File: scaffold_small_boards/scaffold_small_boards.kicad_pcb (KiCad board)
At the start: 2 copper layers, 15 x 15 mm, 36 parts

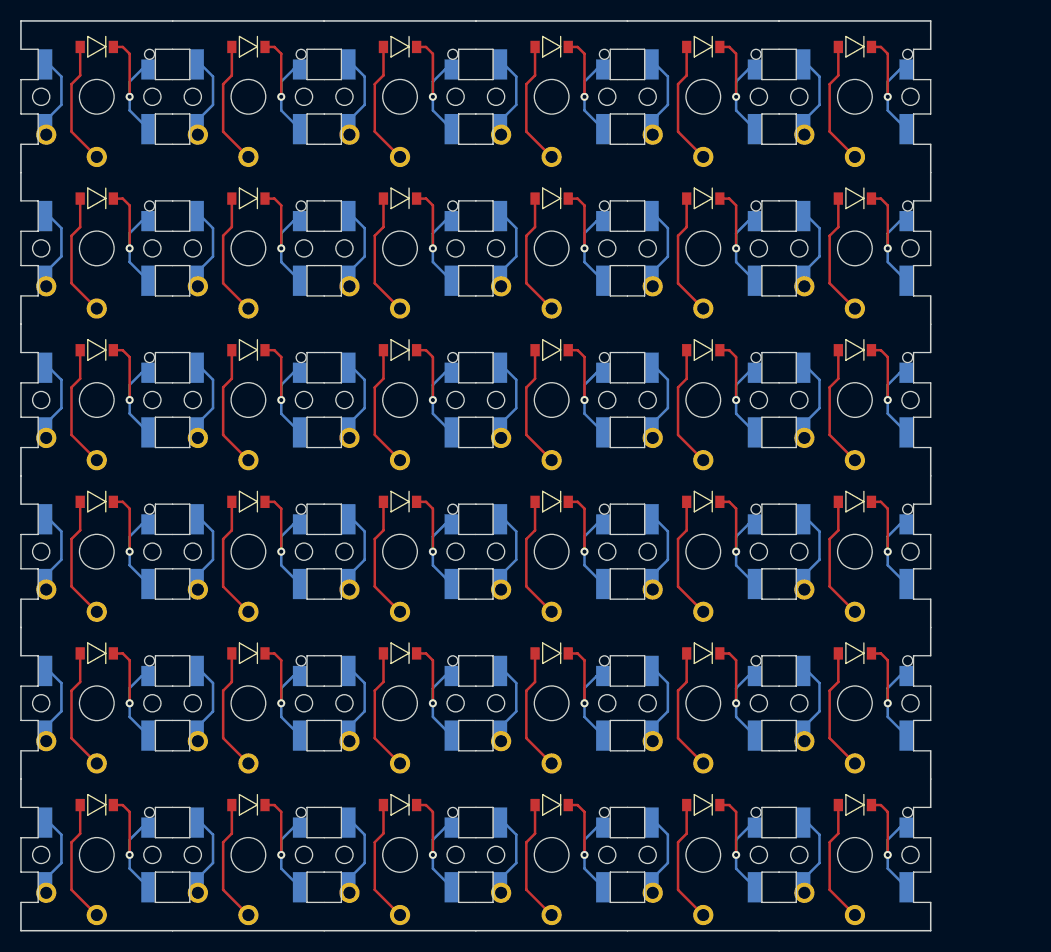
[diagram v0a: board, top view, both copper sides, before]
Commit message: Scaffold V2: wider spacing for supports for better switch fit, updated assembly guide.
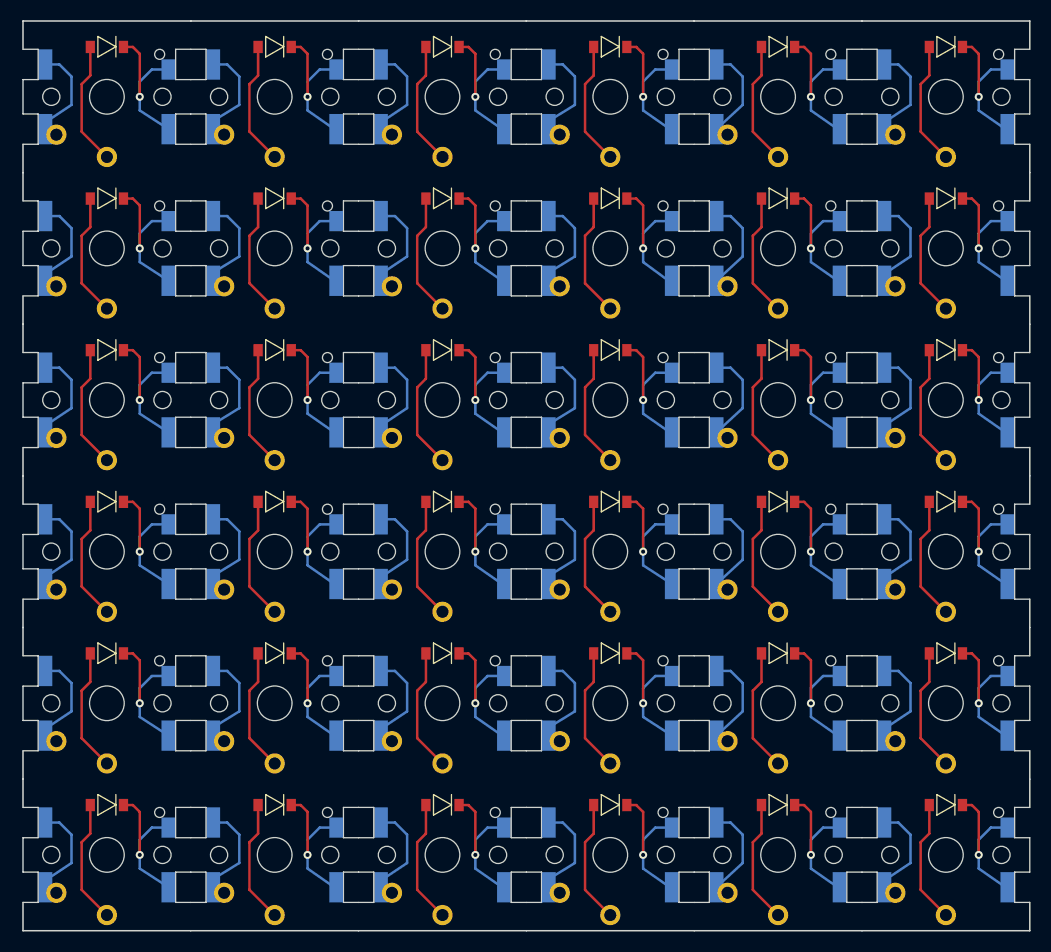
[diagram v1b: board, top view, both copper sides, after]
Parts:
- SW_and_D1: footprint scaffold:Kailh_PG1350_and_sod123_and_cutouts_top_left -> scaffold:Kailh_PG1350_and_sod123_and_cutouts_top_left_v2
- SW_and_D10, SW_and_D15, SW_and_D20, SW_and_D33: footprint scaffold:Kailh_PG1350_and_sod123_and_cutouts_bottom -> scaffold:Kailh_PG1350_and_sod123_and_cutouts_bottom_v2
- SW_and_D11, SW_and_D16, SW_and_D31, SW_and_D6: footprint scaffold:Kailh_PG1350_and_sod123_and_cutouts_top -> scaffold:Kailh_PG1350_and_sod123_and_cutouts_top_v2
- SW_and_D12, SW_and_D13, SW_and_D14, SW_and_D17, SW_and_D18, SW_and_D19, SW_and_D25, SW_and_D26, SW_and_D27, SW_and_D28, SW_and_D29, SW_and_D30, SW_and_D32, SW_and_D7, SW_and_D8, SW_and_D9: footprint scaffold:Kailh_PG1350_and_sod123_and_cutouts_center -> scaffold:Kailh_PG1350_and_sod123_and_cutouts_center_v2
- SW_and_D2, SW_and_D21, SW_and_D3, SW_and_D4: footprint scaffold:Kailh_PG1350_and_sod123_and_cutouts_left -> scaffold:Kailh_PG1350_and_sod123_and_cutouts_left_v2
- SW_and_D22, SW_and_D23, SW_and_D24, SW_and_D35: footprint scaffold:Kailh_PG1350_and_sod123_and_cutouts_right -> scaffold:Kailh_PG1350_and_sod123_and_cutouts_right_v2
- SW_and_D34: footprint scaffold:Kailh_PG1350_and_sod123_and_cutouts_top_right -> scaffold:Kailh_PG1350_and_sod123_and_cutouts_top_right_v2
- SW_and_D36: footprint scaffold:Kailh_PG1350_and_sod123_and_cutouts_bottom_right -> scaffold:Kailh_PG1350_and_sod123_and_cutouts_bottom_right_v2
- SW_and_D5: footprint scaffold:Kailh_PG1350_and_sod123_and_cutouts_bottom_left -> scaffold:Kailh_PG1350_and_sod123_and_cutouts_bottom_left_v2
- moved SW_and_D22 9.00 mm to (91.5, 37.5)
- moved SW_and_D23 9.00 mm to (91.5, 52.5)
- moved SW_and_D24 9.00 mm to (91.5, 67.5)
- moved SW_and_D34 9.00 mm to (91.5, 7.50)
- moved SW_and_D35 9.00 mm to (91.5, 22.5)
- moved SW_and_D36 9.00 mm to (91.5, 82.5)
- moved SW_and_D25 7.40 mm to (74.9, 67.5)
- moved SW_and_D27 7.40 mm to (74.9, 52.5)
- moved SW_and_D29 7.40 mm to (74.9, 37.5)
- moved SW_and_D31 7.40 mm to (74.9, 7.50)
- moved SW_and_D32 7.40 mm to (74.9, 22.5)
- moved SW_and_D33 7.40 mm to (74.9, 82.5)
- moved SW_and_D11 5.80 mm to (58.3, 7.50)
- moved SW_and_D13 5.80 mm to (58.3, 37.5)
- moved SW_and_D17 5.80 mm to (58.3, 52.5)
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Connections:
- SW_and_D1 pad 1: (no net) -> Net-(SW_and_D1-Pad1)
- SW_and_D1 pad 2: (no net) -> Net-(SW_and_D1-Pad2)
- SW_and_D1 pad A: (no net) -> Net-(SW_and_D1-Pad2)
- SW_and_D1 pad K: (no net) -> Net-(SW_and_D1-PadK)
- SW_and_D10 pad 1: (no net) -> Net-(SW_and_D10-Pad1)
- SW_and_D10 pad 2: (no net) -> Net-(SW_and_D10-Pad2)
- SW_and_D10 pad A: (no net) -> Net-(SW_and_D10-Pad2)
- SW_and_D10 pad K: (no net) -> Net-(SW_and_D10-PadK)
- SW_and_D11 pad 1: (no net) -> Net-(SW_and_D11-Pad1)
- SW_and_D11 pad 2: (no net) -> Net-(SW_and_D11-Pad2)
- SW_and_D11 pad A: (no net) -> Net-(SW_and_D11-Pad2)
- SW_and_D11 pad K: (no net) -> Net-(SW_and_D11-PadK)
- SW_and_D12 pad 1: (no net) -> Net-(SW_and_D12-Pad1)
- SW_and_D12 pad 2: (no net) -> Net-(SW_and_D12-Pad2)
- SW_and_D12 pad A: (no net) -> Net-(SW_and_D12-Pad2)
- SW_and_D12 pad K: (no net) -> Net-(SW_and_D12-PadK)
- SW_and_D13 pad 1: (no net) -> Net-(SW_and_D13-Pad1)
- SW_and_D13 pad 2: (no net) -> Net-(SW_and_D13-Pad2)
- SW_and_D13 pad A: (no net) -> Net-(SW_and_D13-Pad2)
- SW_and_D13 pad K: (no net) -> Net-(SW_and_D13-PadK)
- SW_and_D14 pad 1: (no net) -> Net-(SW_and_D14-Pad1)
- SW_and_D14 pad 2: (no net) -> Net-(SW_and_D14-Pad2)
- SW_and_D14 pad A: (no net) -> Net-(SW_and_D14-Pad2)
- SW_and_D14 pad K: (no net) -> Net-(SW_and_D14-PadK)
- SW_and_D15 pad 1: (no net) -> Net-(SW_and_D15-Pad1)
- SW_and_D15 pad 2: (no net) -> Net-(SW_and_D15-Pad2)
- SW_and_D15 pad A: (no net) -> Net-(SW_and_D15-Pad2)
- SW_and_D15 pad K: (no net) -> Net-(SW_and_D15-PadK)
- SW_and_D16 pad 1: (no net) -> Net-(SW_and_D16-Pad1)
- SW_and_D16 pad 2: (no net) -> Net-(SW_and_D16-Pad2)
- SW_and_D16 pad A: (no net) -> Net-(SW_and_D16-Pad2)
- SW_and_D16 pad K: (no net) -> Net-(SW_and_D16-PadK)
- SW_and_D17 pad 1: (no net) -> Net-(SW_and_D17-Pad1)
- SW_and_D17 pad 2: (no net) -> Net-(SW_and_D17-Pad2)
- SW_and_D17 pad A: (no net) -> Net-(SW_and_D17-Pad2)
- SW_and_D17 pad K: (no net) -> Net-(SW_and_D17-PadK)
- SW_and_D18 pad 1: (no net) -> Net-(SW_and_D18-Pad1)
- SW_and_D18 pad 2: (no net) -> Net-(SW_and_D18-Pad2)
- SW_and_D18 pad A: (no net) -> Net-(SW_and_D18-Pad2)
- SW_and_D18 pad K: (no net) -> Net-(SW_and_D18-PadK)
- SW_and_D19 pad 1: (no net) -> Net-(SW_and_D19-Pad1)
- SW_and_D19 pad 2: (no net) -> Net-(SW_and_D19-Pad2)
- SW_and_D19 pad A: (no net) -> Net-(SW_and_D19-Pad2)
- SW_and_D19 pad K: (no net) -> Net-(SW_and_D19-PadK)
- SW_and_D2 pad 1: (no net) -> Net-(SW_and_D2-Pad1)
- SW_and_D2 pad 2: (no net) -> Net-(SW_and_D2-Pad2)
- SW_and_D2 pad A: (no net) -> Net-(SW_and_D2-Pad2)
- SW_and_D2 pad K: (no net) -> Net-(SW_and_D2-PadK)
- SW_and_D20 pad 1: (no net) -> Net-(SW_and_D20-Pad1)
- SW_and_D20 pad 2: (no net) -> Net-(SW_and_D20-Pad2)
- SW_and_D20 pad A: (no net) -> Net-(SW_and_D20-Pad2)
- SW_and_D20 pad K: (no net) -> Net-(SW_and_D20-PadK)
- SW_and_D21 pad 1: (no net) -> Net-(SW_and_D21-Pad1)
- SW_and_D21 pad 2: (no net) -> Net-(SW_and_D21-Pad2)
- SW_and_D21 pad A: (no net) -> Net-(SW_and_D21-Pad2)
- SW_and_D21 pad K: (no net) -> Net-(SW_and_D21-PadK)
- SW_and_D22 pad 1: (no net) -> Net-(SW_and_D22-Pad1)
- SW_and_D22 pad 2: (no net) -> Net-(SW_and_D22-Pad2)
- SW_and_D22 pad A: (no net) -> Net-(SW_and_D22-Pad2)
- SW_and_D22 pad K: (no net) -> Net-(SW_and_D22-PadK)
- SW_and_D23 pad 1: (no net) -> Net-(SW_and_D23-Pad1)
- SW_and_D23 pad 2: (no net) -> Net-(SW_and_D23-Pad2)
- SW_and_D23 pad A: (no net) -> Net-(SW_and_D23-Pad2)
- SW_and_D23 pad K: (no net) -> Net-(SW_and_D23-PadK)
- SW_and_D24 pad 1: (no net) -> Net-(SW_and_D24-Pad1)
- SW_and_D24 pad 2: (no net) -> Net-(SW_and_D24-Pad2)
- SW_and_D24 pad A: (no net) -> Net-(SW_and_D24-Pad2)
- SW_and_D24 pad K: (no net) -> Net-(SW_and_D24-PadK)
- SW_and_D25 pad 1: (no net) -> Net-(SW_and_D25-Pad1)
- SW_and_D25 pad 2: (no net) -> Net-(SW_and_D25-Pad2)
- SW_and_D25 pad A: (no net) -> Net-(SW_and_D25-Pad2)
- SW_and_D25 pad K: (no net) -> Net-(SW_and_D25-PadK)
- SW_and_D26 pad 1: (no net) -> Net-(SW_and_D26-Pad1)
- SW_and_D26 pad 2: (no net) -> Net-(SW_and_D26-Pad2)
- SW_and_D26 pad A: (no net) -> Net-(SW_and_D26-Pad2)
- SW_and_D26 pad K: (no net) -> Net-(SW_and_D26-PadK)
- SW_and_D27 pad 1: (no net) -> Net-(SW_and_D27-Pad1)
- SW_and_D27 pad 2: (no net) -> Net-(SW_and_D27-Pad2)
- SW_and_D27 pad A: (no net) -> Net-(SW_and_D27-Pad2)
- SW_and_D27 pad K: (no net) -> Net-(SW_and_D27-PadK)
- SW_and_D28 pad 1: (no net) -> Net-(SW_and_D28-Pad1)
- SW_and_D28 pad 2: (no net) -> Net-(SW_and_D28-Pad2)
- SW_and_D28 pad A: (no net) -> Net-(SW_and_D28-Pad2)
- SW_and_D28 pad K: (no net) -> Net-(SW_and_D28-PadK)
- SW_and_D29 pad 1: (no net) -> Net-(SW_and_D29-Pad1)
- SW_and_D29 pad 2: (no net) -> Net-(SW_and_D29-Pad2)
- SW_and_D29 pad A: (no net) -> Net-(SW_and_D29-Pad2)
- SW_and_D29 pad K: (no net) -> Net-(SW_and_D29-PadK)
- SW_and_D3 pad 1: (no net) -> Net-(SW_and_D3-Pad1)
- SW_and_D3 pad 2: (no net) -> Net-(SW_and_D3-Pad2)
- SW_and_D3 pad A: (no net) -> Net-(SW_and_D3-Pad2)
- SW_and_D3 pad K: (no net) -> Net-(SW_and_D3-PadK)
- SW_and_D30 pad 1: (no net) -> Net-(SW_and_D30-Pad1)
- SW_and_D30 pad 2: (no net) -> Net-(SW_and_D30-Pad2)
- SW_and_D30 pad A: (no net) -> Net-(SW_and_D30-Pad2)
- SW_and_D30 pad K: (no net) -> Net-(SW_and_D30-PadK)
- SW_and_D31 pad 1: (no net) -> Net-(SW_and_D31-Pad1)
- SW_and_D31 pad 2: (no net) -> Net-(SW_and_D31-Pad2)
- SW_and_D31 pad A: (no net) -> Net-(SW_and_D31-Pad2)
- SW_and_D31 pad K: (no net) -> Net-(SW_and_D31-PadK)
- SW_and_D32 pad 1: (no net) -> Net-(SW_and_D32-Pad1)
- SW_and_D32 pad 2: (no net) -> Net-(SW_and_D32-Pad2)
- SW_and_D32 pad A: (no net) -> Net-(SW_and_D32-Pad2)
- SW_and_D32 pad K: (no net) -> Net-(SW_and_D32-PadK)
- SW_and_D33 pad 1: (no net) -> Net-(SW_and_D33-Pad1)
- SW_and_D33 pad 2: (no net) -> Net-(SW_and_D33-Pad2)
- SW_and_D33 pad A: (no net) -> Net-(SW_and_D33-Pad2)
- SW_and_D33 pad K: (no net) -> Net-(SW_and_D33-PadK)
- SW_and_D34 pad 1: (no net) -> Net-(SW_and_D34-Pad1)
- SW_and_D34 pad 2: (no net) -> Net-(SW_and_D34-Pad2)
- SW_and_D34 pad A: (no net) -> Net-(SW_and_D34-Pad2)
- SW_and_D34 pad K: (no net) -> Net-(SW_and_D34-PadK)
- SW_and_D35 pad 1: (no net) -> Net-(SW_and_D35-Pad1)
- SW_and_D35 pad 2: (no net) -> Net-(SW_and_D35-Pad2)
- SW_and_D35 pad A: (no net) -> Net-(SW_and_D35-Pad2)
- SW_and_D35 pad K: (no net) -> Net-(SW_and_D35-PadK)
- SW_and_D36 pad 1: (no net) -> Net-(SW_and_D36-Pad1)
- SW_and_D36 pad 2: (no net) -> Net-(SW_and_D36-Pad2)
- SW_and_D36 pad A: (no net) -> Net-(SW_and_D36-Pad2)
- SW_and_D36 pad K: (no net) -> Net-(SW_and_D36-PadK)
- SW_and_D4 pad 1: (no net) -> Net-(SW_and_D4-Pad1)
- SW_and_D4 pad 2: (no net) -> Net-(SW_and_D4-Pad2)
- SW_and_D4 pad A: (no net) -> Net-(SW_and_D4-Pad2)
- SW_and_D4 pad K: (no net) -> Net-(SW_and_D4-PadK)
- SW_and_D5 pad 1: (no net) -> Net-(SW_and_D5-Pad1)
- SW_and_D5 pad 2: (no net) -> Net-(SW_and_D5-Pad2)
- SW_and_D5 pad A: (no net) -> Net-(SW_and_D5-Pad2)
- SW_and_D5 pad K: (no net) -> Net-(SW_and_D5-PadK)
- SW_and_D6 pad 1: (no net) -> Net-(SW_and_D6-Pad1)
- SW_and_D6 pad 2: (no net) -> Net-(SW_and_D6-Pad2)
- SW_and_D6 pad A: (no net) -> Net-(SW_and_D6-Pad2)
- SW_and_D6 pad K: (no net) -> Net-(SW_and_D6-PadK)
- SW_and_D7 pad 1: (no net) -> Net-(SW_and_D7-Pad1)
- SW_and_D7 pad 2: (no net) -> Net-(SW_and_D7-Pad2)
- SW_and_D7 pad A: (no net) -> Net-(SW_and_D7-Pad2)
- SW_and_D7 pad K: (no net) -> Net-(SW_and_D7-PadK)
- SW_and_D8 pad 1: (no net) -> Net-(SW_and_D8-Pad1)
- SW_and_D8 pad 2: (no net) -> Net-(SW_and_D8-Pad2)
- SW_and_D8 pad A: (no net) -> Net-(SW_and_D8-Pad2)
- SW_and_D8 pad K: (no net) -> Net-(SW_and_D8-PadK)
- SW_and_D9 pad 1: (no net) -> Net-(SW_and_D9-Pad1)
- SW_and_D9 pad 2: (no net) -> Net-(SW_and_D9-Pad2)
- SW_and_D9 pad A: (no net) -> Net-(SW_and_D9-Pad2)
- SW_and_D9 pad K: (no net) -> Net-(SW_and_D9-PadK)
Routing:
- net (no net): track 1253.8 -> 0.00 mm, vias 36 -> 0
- net Net-(SW_and_D17-PadK): track 0.00 -> 17.0 mm, vias 0 -> 1
- net Net-(SW_and_D19-PadK): track 0.00 -> 17.0 mm, vias 0 -> 1
- net Net-(SW_and_D30-PadK): track 0.00 -> 16.9 mm, vias 0 -> 1
- net Net-(SW_and_D11-PadK): track 0.00 -> 16.8 mm, vias 0 -> 1
- net Net-(SW_and_D20-PadK): track 0.00 -> 16.6 mm, vias 0 -> 1
- net Net-(SW_and_D13-PadK): track 0.00 -> 16.6 mm, vias 0 -> 1
- net Net-(SW_and_D5-PadK): track 0.00 -> 15.7 mm, vias 0 -> 1
- net Net-(SW_and_D3-PadK): track 0.00 -> 15.7 mm, vias 0 -> 1
- net Net-(SW_and_D2-PadK): track 0.00 -> 15.7 mm, vias 0 -> 1
- net Net-(SW_and_D4-PadK): track 0.00 -> 15.7 mm, vias 0 -> 1
- net Net-(SW_and_D21-PadK): track 0.00 -> 15.7 mm, vias 0 -> 1
- net Net-(SW_and_D1-PadK): track 0.00 -> 15.7 mm, vias 0 -> 1
- net Net-(SW_and_D36-PadK): track 0.00 -> 15.4 mm, vias 0 -> 1
- net Net-(SW_and_D23-PadK): track 0.00 -> 15.4 mm, vias 0 -> 1
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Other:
- board size 15 x 15 mm -> 16.6 x 15 mm
